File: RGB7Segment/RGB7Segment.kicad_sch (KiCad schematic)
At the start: 14 parts, among them J1 Conn_01x04_Female, J2 Conn_01x04_Female

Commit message: Slotted/Cut Design Uploaded. Waiting on COnfirmation of Operation
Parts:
- removed D3, D4: SK6812-E, Library:12-23C, symbol LED:WS2812B
- removed J2: Conn_01x04_Female, Connector_PinHeader_2.54mm:PinHeader_1x04_P2.54mm_Vertical, symbol Connector:Conn_01x04_Female
- removed R1, R2: 0, Resistor_SMD:R_0402_1005Metric, symbol Device:R
- added A2, B2, C5, E2, F2, G2: SK6812-E, Library:12-23C, symbol LED:WS2812B
- added C2: 0.470u, Capacitor_SMD:C_0402_1005Metric, symbol Device:C
- added C3, C4, C8, C9: 0.1u, Capacitor_SMD:C_0402_1005Metric, symbol Device:C
- A1, D1: footprint Library:4960_ADA -> Library:12-23C
- B1: footprint Library:4960_Test2 -> Library:12-23C
- C1, G1: footprint Library:4960_Test4 -> Library:12-23C
- E1: footprint Library:4960_Test3 -> Library:12-23C
- F1: footprint Library:4960_Test1 -> Library:12-23C
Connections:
- net D1: now also E1.2 (DOUT); no longer C1.2 (DOUT)
- net D2: now also D2.4 (DIN), E2.2 (DOUT); no longer G1.2 (DOUT)
- net DIN: now also B1.4 (DIN)
- net DOUT: now also J1.3 (Pin_3), G2.2 (DOUT)
- net GND: now also A2.3 (VSS), B2.3 (VSS), C2.2, C3.2, C4.2, C5.3 (VSS), C8.2, C9.2, E2.3 (VSS), F2.3 (VSS), G2.3 (VSS)
- net A1: now reaches B1.2 (DOUT)
- net A1: now also A1.4 (DIN); no longer C1.4 (DIN)
- net F1: now reaches A1.2 (DOUT)
- net F1: now also F1.4 (DIN); no longer B1.4 (DIN)
- net C2: now reaches D2.2 (DOUT)
- net C2: now also C5.4 (DIN)
- net E1: now reaches F1.2 (DOUT)
- net E1: now also E1.4 (DIN); no longer G1.4 (DIN)
- net C1: now reaches D1.2 (DOUT)
- net C1: now also C1.4 (DIN); no longer E1.4 (DIN)
- net +3V3 renamed VCC
- net VCC: now also A2.1 (VDD), B2.1 (VDD), C2.1, C3.1, C4.1, C5.1 (VDD), C8.1, C9.1, E2.1 (VDD), F2.1 (VDD), G2.1 (VDD)
- new net A2: A2.4 (DIN), B2.2 (DOUT)
- new net B2: B2.4 (DIN), C5.2 (DOUT)
- new net E2: E2.4 (DIN), G1.2 (DOUT)
- new net F2: A2.2 (DOUT), F2.4 (DIN)
- new net G1: C1.2 (DOUT), G1.4 (DIN)
- new net G2: F2.2 (DOUT), G2.4 (DIN)
- no-connect marks 6 -> 0
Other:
- moved on the sheet: A1, B1, C1, D1, E1, F1, G1

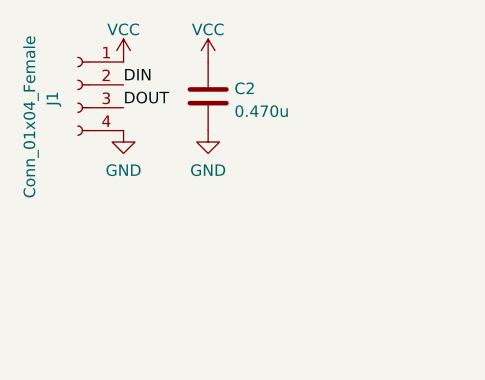
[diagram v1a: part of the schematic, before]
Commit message: Moving Design over to non cutout.
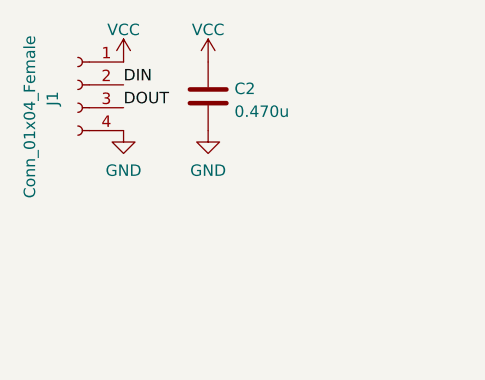
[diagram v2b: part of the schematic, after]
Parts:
- A1, A2, B1, B2, C1, C5, D1, D2, E1, E2, F1, F2, G1, G2: footprint Library:12-23C -> Library:4960_Test4

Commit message: Cleaning up PCB, and minor cleanup.
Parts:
- removed J1: Conn_01x04_Female, Connector_PinHeader_2.54mm:PinHeader_1x04_P2.54mm_Vertical, symbol Connector:Conn_01x04_Female
- added J1, J2: Conn_01x02_Socket, Connector_PinHeader_2.54mm:PinHeader_1x02_P2.54mm_Vertical, symbol Connector:Conn_01x02_Socket
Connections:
- net DIN: now also J2.1 (Pin_1); no longer B1.4 (DIN)
- net DOUT: now also J2.2 (Pin_2); no longer G2.2 (DOUT)
- net GND: now also J1.1 (Pin_1)
- net VCC: now also J1.2 (Pin_2)
- net A1: no longer names the net of B1.2 (DOUT)
- net A1: no longer A1.4 (DIN)
- net A2: no longer names the net of A2.4 (DIN)
- net A2: no longer B2.2 (DOUT)
- net B2: no longer names the net of C5.2 (DOUT)
- net B2: no longer B2.4 (DIN)
- net C1: no longer names the net of C1.4 (DIN)
- net C1: no longer D1.2 (DOUT)
- net C2: no longer names the net of C5.4 (DIN)
- net C2: no longer D2.2 (DOUT)
- net D1: no longer names the net of E1.2 (DOUT)
- net D1: no longer D1.4 (DIN)
- net D2: no longer names the net of D2.4 (DIN)
- net D2: no longer E2.2 (DOUT)
- net E1: no longer names the net of F1.2 (DOUT)
- net E1: no longer E1.4 (DIN)
- net E2: no longer names the net of G1.2 (DOUT)
- net E2: no longer E2.4 (DIN)
- net F1: no longer names the net of F1.4 (DIN)
- net F1: no longer A1.2 (DOUT)
- net F2: no longer names the net of A2.2 (DOUT)
- net F2: no longer F2.4 (DIN)
- net G1: no longer names the net of C1.2 (DOUT)
- net G1: no longer G1.4 (DIN)
- net G2: no longer names the net of G2.4 (DIN)
- net G2: no longer F2.2 (DOUT)
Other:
- moved on the sheet: C2

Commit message: Adding New Models,
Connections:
- net DIN: now also C1.4 (DIN)
- net DOUT: now also E2.2 (DOUT)
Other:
- moved on the sheet: C1, E2
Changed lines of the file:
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@@
 		)
 	)
-	(label "DIN"
-		(at 179.07 143.51 0)
+	(label "DOUT"
+		(at 101.6 157.48 0)
 		(fields_autoplaced yes)
 		(effects
@@
 	)
 	(label "DOUT"
-		(at 179.07 146.05 0)
+		(at 26.67 35.56 0)
 		(fields_autoplaced yes)
 		(effects
@@
 		)
 	)
-	(label "DOUT"
-		(at 26.67 35.56 0)
+	(label "DIN"
+		(at 179.07 52.07 180)
 		(fields_autoplaced yes)
 		(effects
@@
 				(size 1.27 1.27)
 			)
-			(justify left bottom)
+			(justify right bottom)
 		)
 	)
 	(symbol
 		(lib_id "power:VCC")
-		(at 180.34 45.974 0)
+		(at 186.69 44.45 0)
 		(unit 1)
 		(exclude_from_sim no)
@@
 		(fields_autoplaced yes)
 		(property "Reference" "#PWR0117"
-			(at 180.34 49.784 0)
+			(at 186.69 48.26 0)
 			(effects
 				(font
@@
 		)
 		(property "Value" "VCC"
-			(at 180.34 42.3982 0)
+			(at 186.69 40.8742 0)
 			(effects
 				(font
@@
 		)
 		(property "Footprint" ""
-			(at 180.34 45.974 0)
-			(effects
-				(font
-					(size 1.27 1.27)
-				)
-				(hide yes)
-			)
-		)
-		(property "Datasheet" ""
-			(at 180.34 45.974 0)
-			(effects
-				(font
-					(size 1.27 1.27)
-				)
-				(hide yes)
-			)
-		)
-		(property "Description" ""
-			(at 180.34 45.974 0)
+			(at 186.69 44.45 0)
+			(effects
+				(font
+					(size 1.27 1.27)
+				)
+				(hide yes)
+			)
+		)
+		(property "Datasheet" ""
+			(at 186.69 44.45 0)
+			(effects
+				(font
+					(size 1.27 1.27)
+				)
+				(hide yes)
+			)
+		)
+		(property "Description" ""
+			(at 186.69 44.45 0)
 			(effects
 				(font
@@
 	(symbol
 		(lib_id "LED:WS2812B")
-		(at 180.34 53.594 0)
+		(at 186.69 52.07 0)
 		(unit 1)
 		(exclude_from_sim no)
@@
 		(dnp no)
 		(property "Reference" "C1"
-			(at 190.6459 50.1356 0)
+			(at 196.9959 48.6116 0)
 			(effects
 				(font
@@
 		)
 		(property "Value" "SK6812-E"
-			(at 192.532 59.69 0)
+			(at 198.882 58.166 0)
 			(effects
 				(font
@@
 		)
 		(property "Footprint" "Library:4960_Test4"
-			(at 181.61 61.214 0)
+			(at 187.96 59.69 0)
 			(effects
 				(font
@@
 		)
 		(property "Datasheet" ""
-			(at 182.88 63.119 0)
+			(at 189.23 61.595 0)
 			(effects
 				(font
@@
 		)
 		(property "Description" ""
-			(at 180.34 53.594 0)
+			(at 186.69 52.07 0)
 			(effects
 				(font
@@
 	(symbol
 		(lib_id "power:GND")
-		(at 93.98 164.338 0)
+		(at 93.98 165.1 0)
 		(mirror y)
 		(unit 1)
@@
 		(fields_autoplaced yes)
 		(property "Reference" "#PWR0137"
-			(at 93.98 170.688 0)
+			(at 93.98 171.45 0)
 			(effects
 				(font
@@
 		)
 		(property "Value" "GND"
-			(at 93.98 168.7814 0)
+			(at 93.98 169.5434 0)
 			(effects
 				(font
@@
 		)
 		(property "Footprint" ""
-			(at 93.98 164.338 0)
-			(effects
-				(font
-					(size 1.27 1.27)
-				)
-				(hide yes)
-			)
-		)
-		(property "Datasheet" ""
-			(at 93.98 164.338 0)
-			(effects
-				(font
-					(size 1.27 1.27)
-				)
-				(hide yes)
-			)
-		)
-		(property "Description" ""
-			(at 93.98 164.338 0)
+			(at 93.98 165.1 0)
+			(effects
+				(font
+					(size 1.27 1.27)
+				)
+				(hide yes)
+			)
+		)
+		(property "Datasheet" ""
+			(at 93.98 165.1 0)
+			(effects
+				(font
+					(size 1.27 1.27)
+				)
+				(hide yes)
+			)
+		)
+		(property "Description" ""
+			(at 93.98 165.1 0)
 			(effects
 				(font
@@
 	(symbol
 		(lib_id "LED:WS2812B")
-		(at 93.98 156.718 0)
+		(at 93.98 157.48 0)
 		(unit 1)
 		(exclude_from_sim no)
@@
 		(dnp no)
 		(property "Reference" "E2"
-			(at 104.2859 153.2596 0)
+			(at 104.2859 154.0216 0)
 			(effects
 				(font
@@
 		)
 		(property "Value" "SK6812-E"
-			(at 106.172 162.814 0)
+			(at 106.172 163.576 0)
 			(effects
 				(font
@@
 		)
 		(property "Footprint" "Library:4960_Test4"
-			(at 95.25 164.338 0)
+			(at 95.25 165.1 0)
 			(effects
 				(font
@@
 		)
 		(property "Datasheet" ""
-			(at 96.52 166.243 0)
+			(at 96.52 167.005 0)
 			(effects
 				(font
@@
 		)
 		(property "Description" ""
-			(at 93.98 156.718 0)
+			(at 93.98 157.48 0)
 			(effects
 				(font
@@
 	(symbol
 		(lib_id "power:VCC")
-		(at 93.98 149.098 0)
+		(at 93.98 149.86 0)
 		(unit 1)
 		(exclude_from_sim no)
@@
 		(fields_autoplaced yes)
 		(property "Reference" "#PWR0140"
-			(at 93.98 152.908 0)
+			(at 93.98 153.67 0)
 			(effects
 				(font
@@
 		)
 		(property "Value" "VCC"
-			(at 93.98 145.5222 0)
+			(at 93.98 146.2842 0)
 			(effects
 				(font
@@
 		)
 		(property "Footprint" ""
-			(at 93.98 149.098 0)
-			(effects
-				(font
-					(size 1.27 1.27)
-				)
-				(hide yes)
-			)
-		)
-		(property "Datasheet" ""
-			(at 93.98 149.098 0)
-			(effects
-				(font
-					(size 1.27 1.27)
-				)
-				(hide yes)
-			)
-		)
-		(property "Description" ""
-			(at 93.98 149.098 0)
+			(at 93.98 149.86 0)
+			(effects
+				(font
+					(size 1.27 1.27)
+				)
+				(hide yes)
+			)
+		)
+		(property "Datasheet" ""
+			(at 93.98 149.86 0)
+			(effects
+				(font
+					(size 1.27 1.27)
+				)
+				(hide yes)
+			)
+		)
+		(property "Description" ""
+			(at 93.98 149.86 0)
 			(effects
 				(font
@@
 	(symbol
 		(lib_id "power:GND")
-		(at 180.34 61.214 0)
+		(at 186.69 59.69 0)
 		(mirror y)
 		(unit 1)
@@
 		(fields_autoplaced yes)
 		(property "Reference" "#PWR0108"
-			(at 180.34 67.564 0)
+			(at 186.69 66.04 0)
 			(effects
 				(font
@@
 		)
 		(property "Value" "GND"
-			(at 180.34 65.6574 0)
+			(at 186.69 64.1334 0)
 			(effects
 				(font
@@
 		)
 		(property "Footprint" ""
-			(at 180.34 61.214 0)
-			(effects
-				(font
-					(size 1.27 1.27)
-				)
-				(hide yes)
-			)
-		)
-		(property "Datasheet" ""
-			(at 180.34 61.214 0)
-			(effects
-				(font
-					(size 1.27 1.27)
-				)
-				(hide yes)
-			)
-		)
-		(property "Description" ""
-			(at 180.34 61.214 0)
-			(effects
-				(font
+			(at 186.69 59.69 0)
+			(effects
+				(font
+					(size 1.27 1.27)
+				)
+				(hide yes)
+			)
+		)
+		(property "Datasheet" ""
+			(at 186.69 59.69 0)
+			(effects
+				(font
+					(size 1.27 1.27)
+				)
+				(hide yes)
+			)
+		)
+		(property "Description" ""
+			(at 186.69 59.69 0)
+			(effects
+				(font

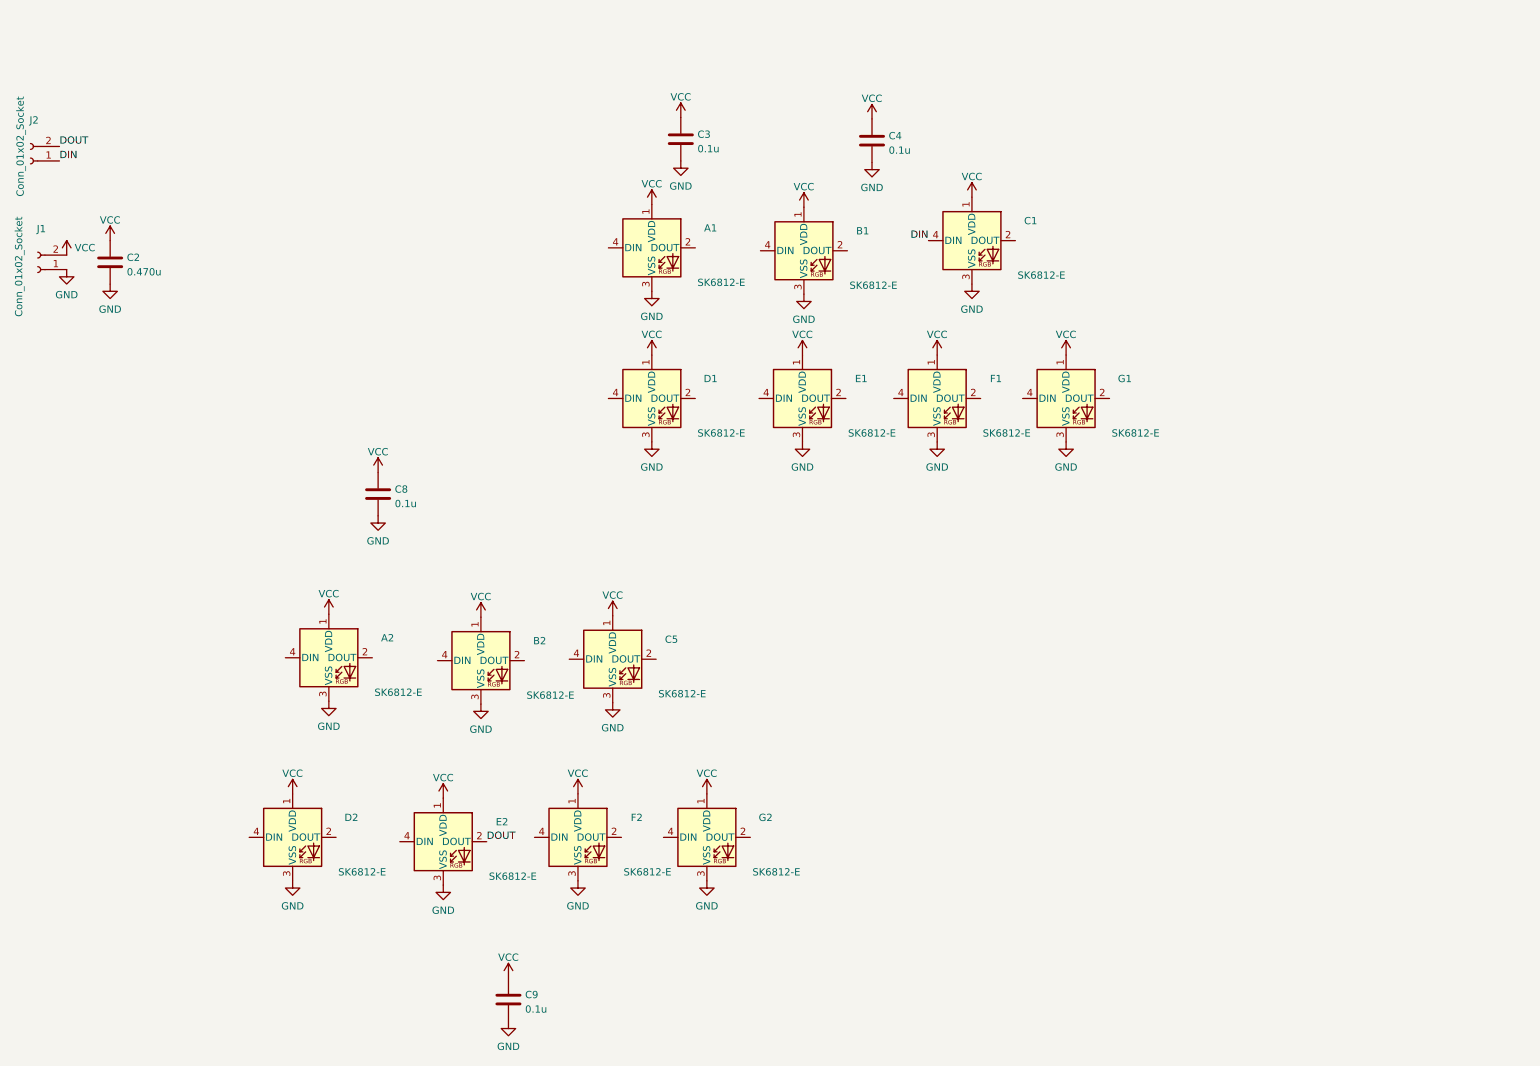
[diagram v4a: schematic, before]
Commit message: Smaller Size first pass layout
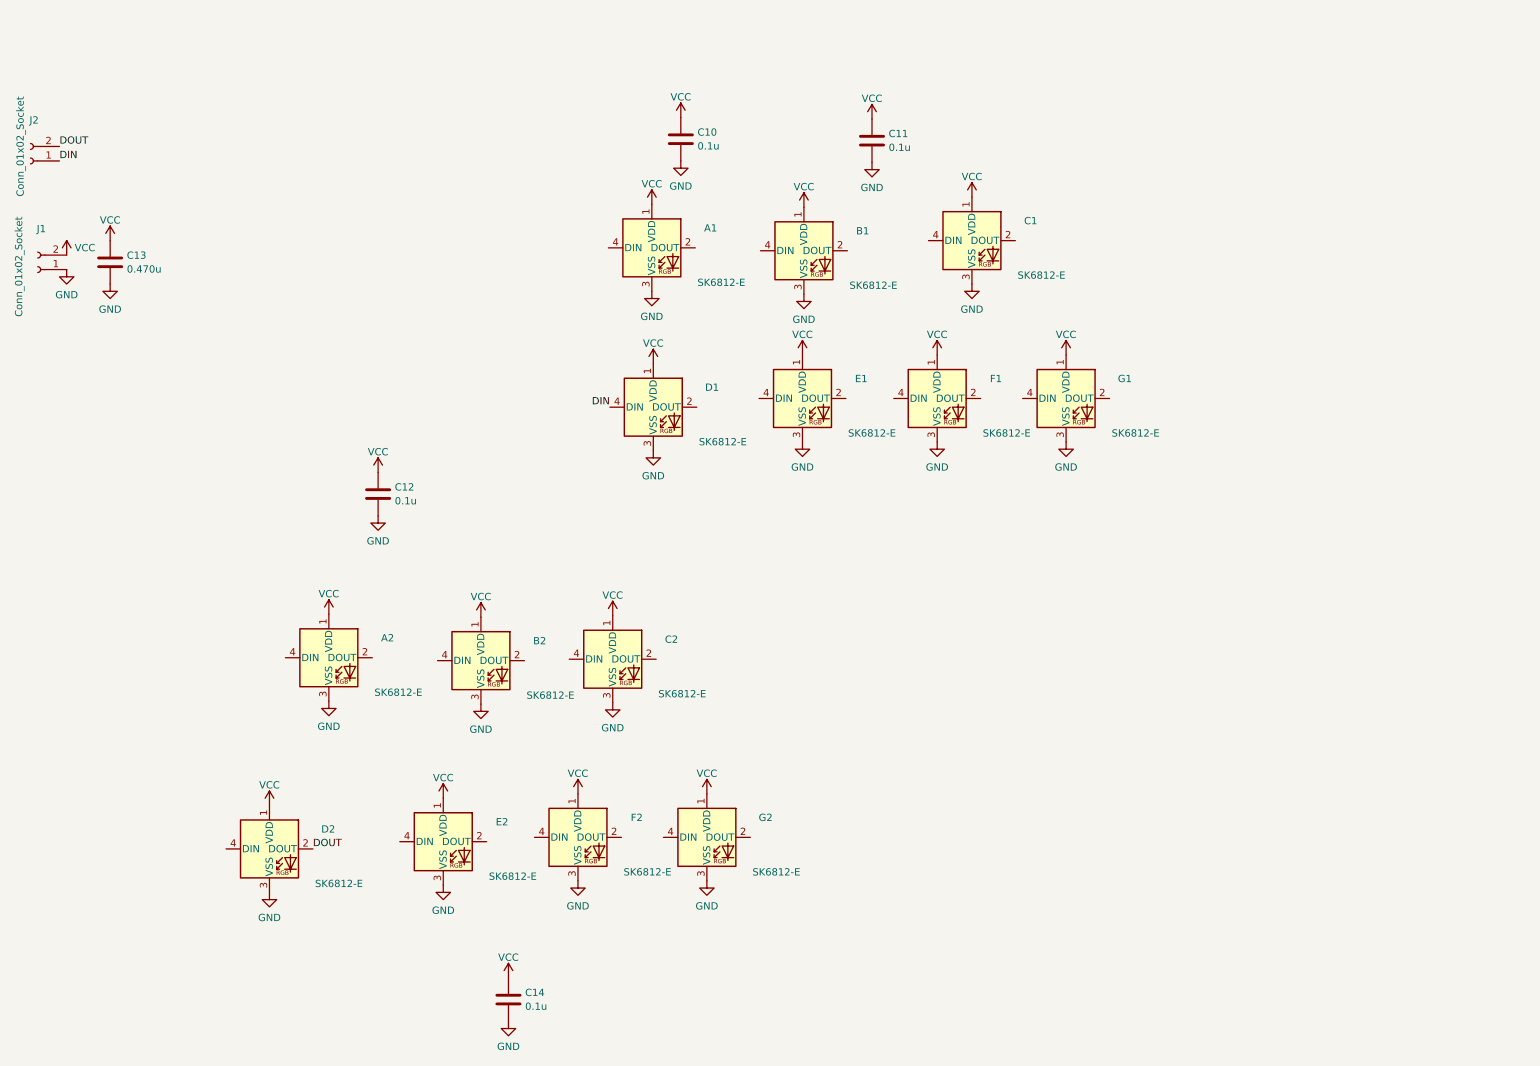
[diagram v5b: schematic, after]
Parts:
- A1, A2, B1, B2, C1, D1, D2, E1, E2, F1, F2, G1, G2: footprint Library:4960_Test4 -> Library:12-23C
- C2: renamed from C5; footprint Library:4960_Test4 -> Library:12-23C
- J1, J2: footprint Connector_PinHeader_2.54mm:PinHeader_1x02_P2.54mm_Vertical -> Connector_PinHeader_1.27mm:PinHeader_1x02_P1.27mm_Vertical
- renumbered C3 to C10, C4 to C11, C8 to C12, C2 to C13, C9 to C14
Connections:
- net DIN: now also D1.4 (DIN); no longer C1.4 (DIN)
- net DOUT: now also D2.2 (DOUT); no longer E2.2 (DOUT)
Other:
- moved on the sheet: D1, D2

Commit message: New Pass of RGB 7 Segment
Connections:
- net E2: now reaches C1.2 (DOUT)
- net E2: now also E2.4 (DIN)
- net at C1.4 (DIN): now also G1.2 (DOUT)
- net at A2.2 (DOUT): now also B2.4 (DIN)
- net at A2.4 (DIN): now also F2.2 (DOUT)
- net at B1.2 (DOUT): now also G1.4 (DIN)
- net at B1.4 (DIN): now also A1.2 (DOUT)
- net at C2.2 (DOUT): now also G2.4 (DIN)
- net at C2.4 (DIN): now also B2.2 (DOUT)
- net at D2.4 (DIN): now also G2.2 (DOUT)
- net at F1.2 (DOUT): now also A1.4 (DIN)
- net at F1.4 (DIN): now also E1.2 (DOUT)
- net at E2.2 (DOUT): now also F2.4 (DIN)
- net at E1.4 (DIN): now also D1.2 (DOUT)
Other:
- moved on the sheet: A1, A2, B1, B2, C1, C2, D1, D2, E1, E2, F1, F2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
